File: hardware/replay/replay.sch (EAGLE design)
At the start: 19 parts, among them J1 SQUALL_HEADER, J2 5.5x2.1mm Barrel, U1 LT3083, U2 LT3083, U3 MAX5483

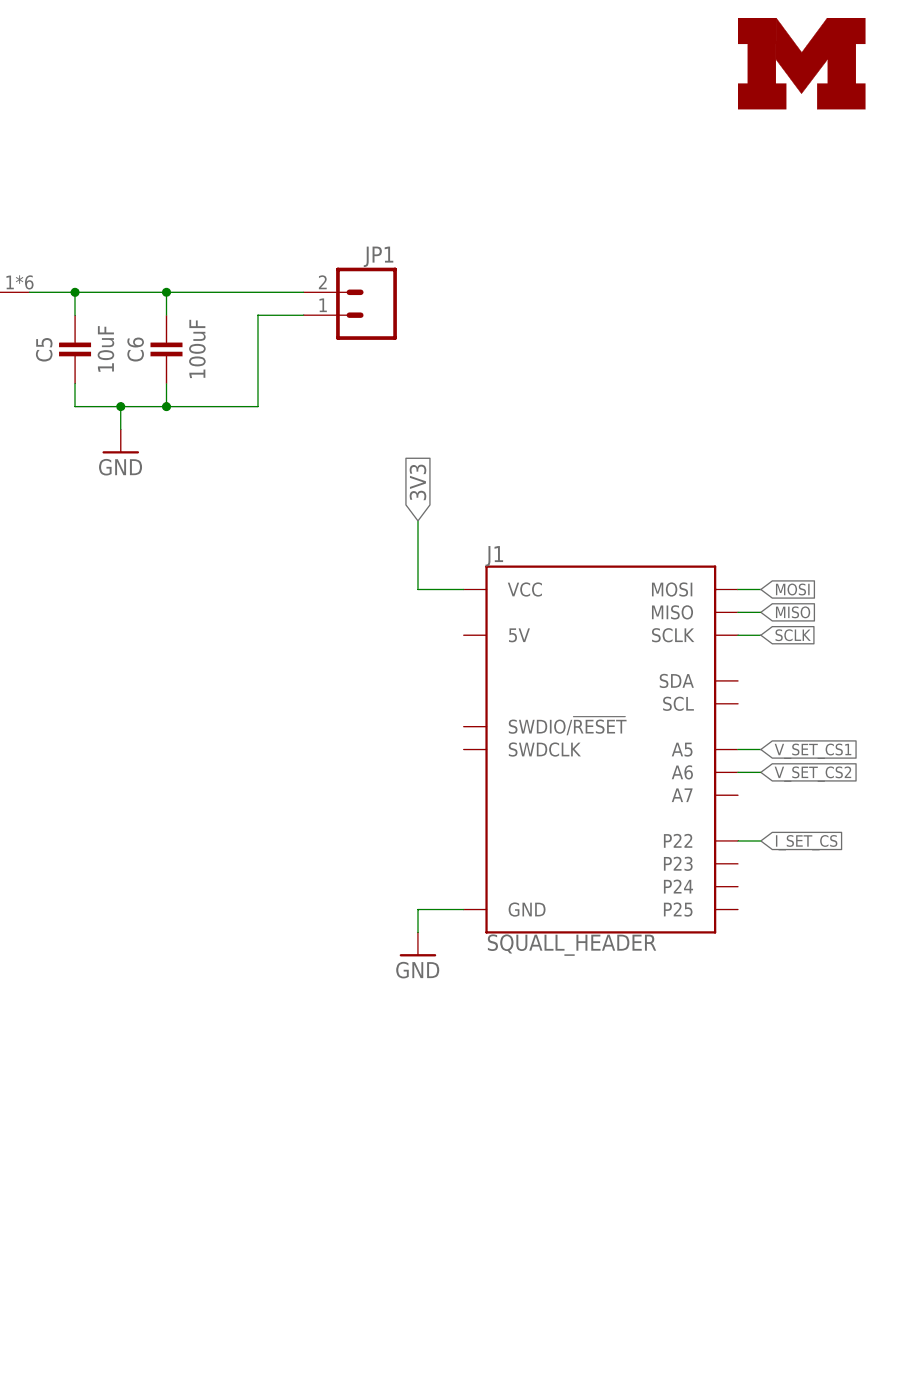
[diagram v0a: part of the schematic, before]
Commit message: board layed out with switches
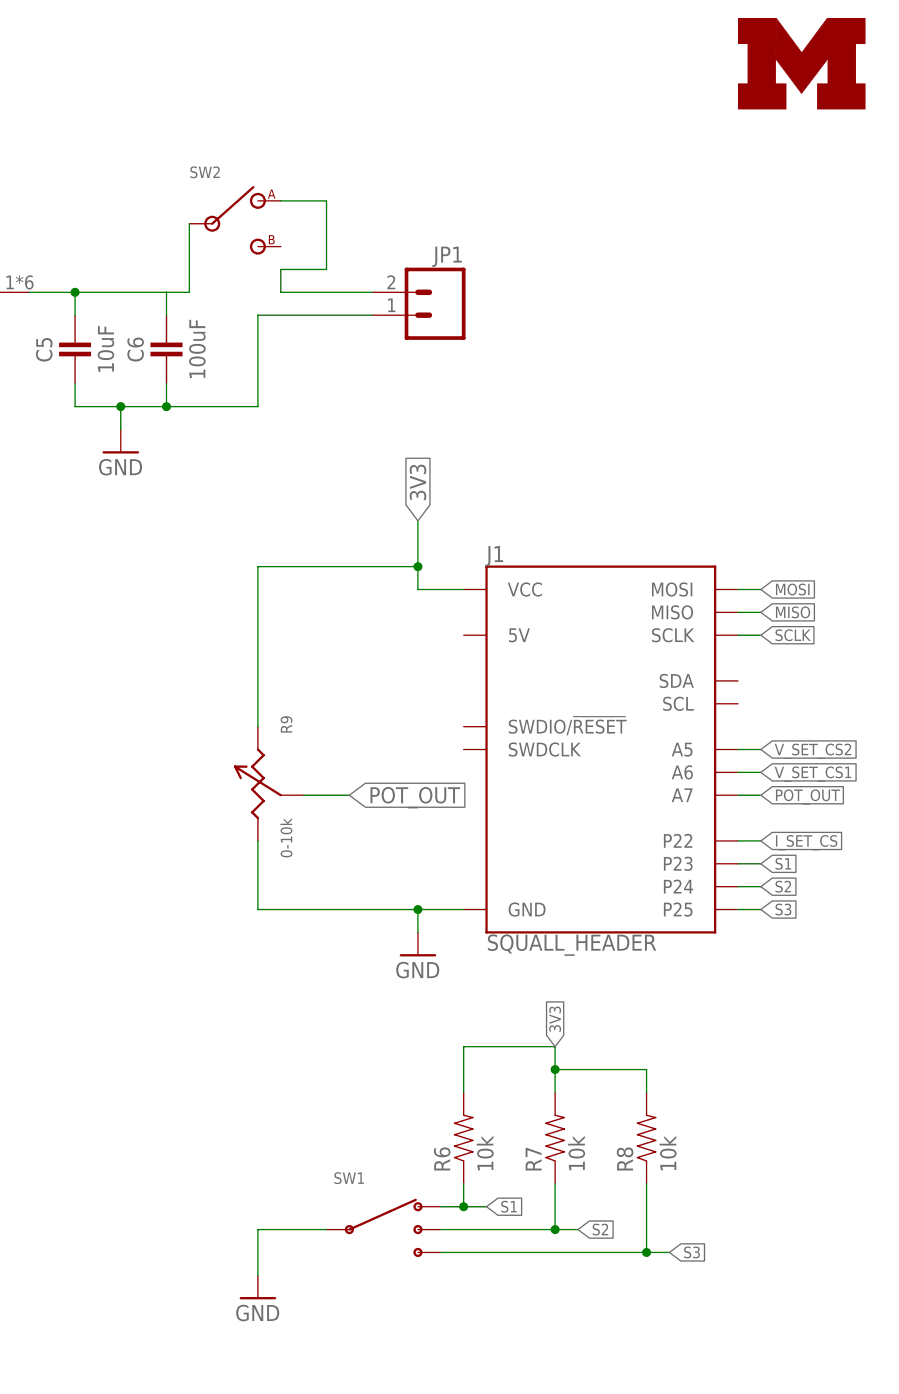
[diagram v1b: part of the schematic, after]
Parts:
- added R6, R7, R8: 10k, passives:RESISTOR
- added R9: 0-10k, pots:POT
- added SW1: CSS-1310TB, switches:CSS-1310TB
- added SW2: 500ASSP, switches:500ASSP
- U3: value MAX5483 -> (none)
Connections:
- new net OUTS: JP1.2, SW2.1
- new net POT_OUT: J1.A7, R9.2
- new net S1: J1.P23, R6.1, SW1.3
- new net S2: J1.P24, R7.1, SW1.2
- new net S3: J1.P25, R8.1, SW1.1
- net 3V3: now also R6.2, R7.2, R8.2, R9.1
- net GND: now also R9.3, SW1.C
- net OUT: now also SW2.2; no longer JP1.2
- net V_SET_CS1: now also J1.A6; no longer J1.A5
- net V_SET_CS2: now also J1.A5; no longer J1.A6
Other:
- moved on the sheet: JP1
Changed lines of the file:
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@@
 <part name="GND9" library="supply1" deviceset="GND" device=""/>
 <part name="JP1" library="SparkFun-Connectors" deviceset="M02" device="5MM"/>
+<part name="SW2" library="switches" deviceset="500ASSP" device=""/>
+<part name="R9" library="pots" deviceset="POT" device="" value="0-10k"/>
+<part name="SW1" library="switches" deviceset="CSS-1310TB" device=""/>
+<part name="GND10" library="supply1" deviceset="GND" device=""/>
+<part name="R6" library="passives" deviceset="RESISTOR" device="" value="10k"/>
+<part name="R7" library="passives" deviceset="RESISTOR" device="" value="10k"/>
+<part name="R8" library="passives" deviceset="RESISTOR" device="" value="10k"/>
 </parts>
 <sheets>
@@
 <instance part="GND8" gate="1" x="116.84" y="142.24"/>
 <instance part="GND9" gate="1" x="162.56" y="134.62"/>
-<instance part="JP1" gate="G$1" x="190.5" y="149.86" rot="MR0"/>
+<instance part="JP1" gate="G$1" x="198.12" y="149.86" rot="MR0"/>
+<instance part="SW2" gate="G$1" x="172.72" y="160.02"/>
+<instance part="R9" gate="G$1" x="177.8" y="99.06" rot="R270"/>
+<instance part="SW1" gate="G$1" x="187.96" y="48.26"/>
+<instance part="GND10" gate="1" x="177.8" y="40.64"/>
+<instance part="R6" gate="G$1" x="200.66" y="58.42" rot="R90"/>
+<instance part="R7" gate="G$1" x="210.82" y="58.42" rot="R90"/>
+<instance part="R8" gate="G$1" x="220.98" y="58.42" rot="R90"/>
 </instances>
 <busses>
@@
 <wire x1="195.58" y1="83.82" x2="195.58" y2="81.28" width="0.1524" layer="91"/>
 <pinref part="GND5" gate="1" pin="GND"/>
+<pinref part="R9" gate="G$1" pin="3"/>
+<wire x1="177.8" y1="91.44" x2="177.8" y2="83.82" width="0.1524" layer="91"/>
+<wire x1="177.8" y1="83.82" x2="195.58" y2="83.82" width="0.1524" layer="91"/>
+<junction x="195.58" y="83.82"/>
 </segment>
 <segment>
@@
 <junction x="167.64" y="139.7"/>
 <pinref part="JP1" gate="G$1" pin="1"/>
-<wire x1="177.8" y1="149.86" x2="182.88" y2="149.86" width="0.1524" layer="91"/>
+<wire x1="177.8" y1="149.86" x2="190.5" y2="149.86" width="0.1524" layer="91"/>
+</segment>
+<segment>
+<pinref part="GND10" gate="1" pin="GND"/>
+<wire x1="177.8" y1="43.18" x2="177.8" y2="48.26" width="0.1524" layer="91"/>
+<pinref part="SW1" gate="G$1" pin="C"/>
+<wire x1="177.8" y1="48.26" x2="185.42" y2="48.26" width="0.1524" layer="91"/>
 </segment>
 </net>
@@
 <pinref part="J1" gate="G$1" pin="VCC"/>
 <wire x1="200.66" y1="119.38" x2="195.58" y2="119.38" width="0.1524" layer="91"/>
-<wire x1="195.58" y1="119.38" x2="195.58" y2="127" width="0.1524" layer="91"/>
+<wire x1="195.58" y1="119.38" x2="195.58" y2="121.92" width="0.1524" layer="91"/>
 <label x="195.58" y="127" size="1.778" layer="95" rot="R90" xref="yes"/>
+<pinref part="R9" gate="G$1" pin="1"/>
+<wire x1="195.58" y1="121.92" x2="195.58" y2="127" width="0.1524" layer="91"/>
+<wire x1="177.8" y1="104.14" x2="177.8" y2="121.92" width="0.1524" layer="91"/>
+<wire x1="177.8" y1="121.92" x2="195.58" y2="121.92" width="0.1524" layer="91"/>
+<junction x="195.58" y="121.92"/>
 </segment>
 <segment>
 <pinref part="R5" gate="G$1" pin="2"/>
 <wire x1="22.86" y1="129.54" x2="22.86" y2="132.08" width="0.1524" layer="91"/>
+</segment>
+<segment>
+<pinref part="R8" gate="G$1" pin="2"/>
+<wire x1="220.98" y1="63.5" x2="220.98" y2="66.04" width="0.1524" layer="91"/>
+<pinref part="R6" gate="G$1" pin="2"/>
+<wire x1="200.66" y1="63.5" x2="200.66" y2="68.58" width="0.1524" layer="91"/>
+<wire x1="200.66" y1="68.58" x2="210.82" y2="68.58" width="0.1524" layer="91"/>
+<pinref part="R7" gate="G$1" pin="2"/>
+<wire x1="210.82" y1="68.58" x2="210.82" y2="66.04" width="0.1524" layer="91"/>
+<wire x1="210.82" y1="66.04" x2="210.82" y2="63.5" width="0.1524" layer="91"/>
+<wire x1="220.98" y1="66.04" x2="210.82" y2="66.04" width="0.1524" layer="91"/>
+<junction x="210.82" y="66.04"/>
+<label x="210.82" y="68.58" size="1.27" layer="95" rot="R90" xref="yes"/>
 </segment>
 </net>
@@
 </segment>
 <segment>
+<pinref part="J1" gate="G$1" pin="A6"/>
+<wire x1="231.14" y1="99.06" x2="233.68" y2="99.06" width="0.1524" layer="91"/>
+<label x="233.68" y="99.06" size="1.27" layer="95" xref="yes"/>
+</segment>
+</net>
+<net name="V_SET_CS2" class="0">
+<segment>
+<pinref part="R3" gate="G$1" pin="!CS"/>
+<wire x1="109.22" y1="71.12" x2="106.68" y2="71.12" width="0.1524" layer="91"/>
+<label x="106.68" y="71.12" size="1.778" layer="95" rot="R180" xref="yes"/>
+</segment>
+<segment>
 <pinref part="J1" gate="G$1" pin="A5"/>
 <wire x1="231.14" y1="101.6" x2="233.68" y2="101.6" width="0.1524" layer="91"/>
 <label x="233.68" y="101.6" size="1.27" layer="95" xref="yes"/>
-</segment>
-</net>
-<net name="V_SET_CS2" class="0">
-<segment>
-<pinref part="R3" gate="G$1" pin="!CS"/>
-<wire x1="109.22" y1="71.12" x2="106.68" y2="71.12" width="0.1524" layer="91"/>
-<label x="106.68" y="71.12" size="1.778" layer="95" rot="R180" xref="yes"/>
-</segment>
-<segment>
-<pinref part="J1" gate="G$1" pin="A6"/>
-<wire x1="231.14" y1="99.06" x2="233.68" y2="99.06" width="0.1524" layer="91"/>
-<label x="233.68" y="99.06" size="1.27" layer="95" xref="yes"/>
 </segment>
 </net>
@@
 <pinref part="C6" gate="G$1" pin="1"/>
 <wire x1="167.64" y1="149.86" x2="167.64" y2="152.4" width="0.1524" layer="91"/>
-<pinref part="JP1" gate="G$1" pin="2"/>
-<wire x1="167.64" y1="152.4" x2="182.88" y2="152.4" width="0.1524" layer="91"/>
-<junction x="167.64" y="152.4"/>
+<wire x1="167.64" y1="152.4" x2="170.18" y2="152.4" width="0.1524" layer="91"/>
+<wire x1="170.18" y1="152.4" x2="170.18" y2="160.02" width="0.1524" layer="91"/>
+<pinref part="SW2" gate="G$1" pin="2"/>
 </segment>
 </net>
@@
 </segment>
 </net>
+<net name="OUTS" class="0">
+<segment>
+<wire x1="180.34" y1="162.56" x2="185.42" y2="162.56" width="0.1524" layer="91"/>
+<wire x1="185.42" y1="162.56" x2="185.42" y2="154.94" width="0.1524" layer="91"/>
+<wire x1="185.42" y1="154.94" x2="180.34" y2="154.94" width="0.1524" layer="91"/>
+<wire x1="180.34" y1="154.94" x2="180.34" y2="152.4" width="0.1524" layer="91"/>
+<pinref part="JP1" gate="G$1" pin="2"/>
+<wire x1="180.34" y1="152.4" x2="190.5" y2="152.4" width="0.1524" layer="91"/>
+<pinref part="SW2" gate="G$1" pin="1"/>
+</segment>
+</net>
+<net name="POT_OUT" class="0">
+<segment>
+<wire x1="182.88" y1="96.52" x2="187.96" y2="96.52" width="0.1524" layer="91"/>
+<label x="187.96" y="96.52" size="1.778" layer="95" xref="yes"/>
+<pinref part="R9" gate="G$1" pin="2"/>
+</segment>
+<segment>
+<pinref part="J1" gate="G$1" pin="A7"/>
+<wire x1="231.14" y1="96.52" x2="233.68" y2="96.52" width="0.1524" layer="91"/>
+<label x="233.68" y="96.52" size="1.27" layer="95" xref="yes"/>
+</segment>
+</net>
+<net name="S1" class="0">
+<segment>
+<pinref part="SW1" gate="G$1" pin="3"/>
+<wire x1="198.12" y1="50.8" x2="200.66" y2="50.8" width="0.1524" layer="91"/>
+<label x="203.2" y="50.8" size="1.27" layer="95" xref="yes"/>
+<pinref part="R6" gate="G$1" pin="1"/>
+<wire x1="200.66" y1="50.8" x2="203.2" y2="50.8" width="0.1524" layer="91"/>
+<wire x1="200.66" y1="53.34" x2="200.66" y2="50.8" width="0.1524" layer="91"/>
+<junction x="200.66" y="50.8"/>
+</segment>
+<segment>
+<pinref part="J1" gate="G$1" pin="P23"/>
+<wire x1="231.14" y1="88.9" x2="233.68" y2="88.9" width="0.1524" layer="91"/>
+<label x="233.68" y="88.9" size="1.27" layer="95" xref="yes"/>
+</segment>
+</net>
+<net name="S2" class="0">
+<segment>
+<pinref part="SW1" gate="G$1" pin="2"/>
+<wire x1="198.12" y1="48.26" x2="210.82" y2="48.26" width="0.1524" layer="91"/>
+<label x="213.36" y="48.26" size="1.27" layer="95" xref="yes"/>
+<pinref part="R7" gate="G$1" pin="1"/>
+<wire x1="210.82" y1="48.26" x2="213.36" y2="48.26" width="0.1524" layer="91"/>
+<wire x1="210.82" y1="53.34" x2="210.82" y2="48.26" width="0.1524" layer="91"/>
+<junction x="210.82" y="48.26"/>
+</segment>
+<segment>
+<pinref part="J1" gate="G$1" pin="P24"/>
+<wire x1="231.14" y1="86.36" x2="233.68" y2="86.36" width="0.1524" layer="91"/>
+<label x="233.68" y="86.36" size="1.27" layer="95" xref="yes"/>
+</segment>
+</net>
+<net name="S3" class="0">
+<segment>
+<pinref part="SW1" gate="G$1" pin="1"/>
+<wire x1="198.12" y1="45.72" x2="220.98" y2="45.72" width="0.1524" layer="91"/>
+<label x="223.52" y="45.72" size="1.27" layer="95" xref="yes"/>
+<pinref part="R8" gate="G$1" pin="1"/>
+<wire x1="220.98" y1="45.72" x2="223.52" y2="45.72" width="0.1524" layer="91"/>
+<wire x1="220.98" y1="53.34" x2="220.98" y2="45.72" width="0.1524" layer="91"/>
+<junction x="220.98" y="45.72"/>
+</segment>
+<segment>
+<pinref part="J1" gate="G$1" pin="P25"/>
+<wire x1="231.14" y1="83.82" x2="233.68" y2="83.82" width="0.1524" layer="91"/>
+<label x="233.68" y="83.82" size="1.27" layer="95" xref="yes"/>
+</segment>
+</net>

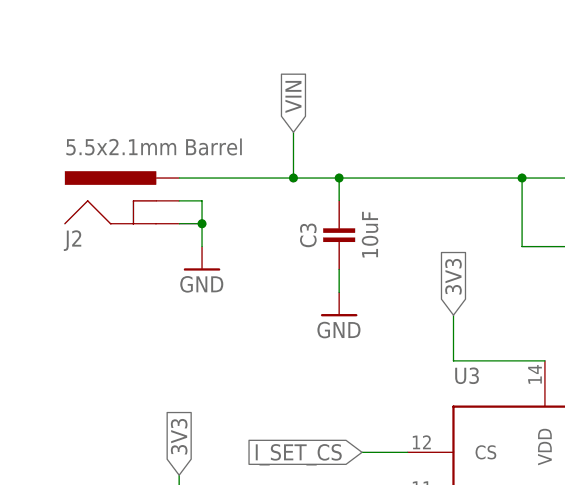
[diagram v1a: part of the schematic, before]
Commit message: updated parts on the board and started making a case
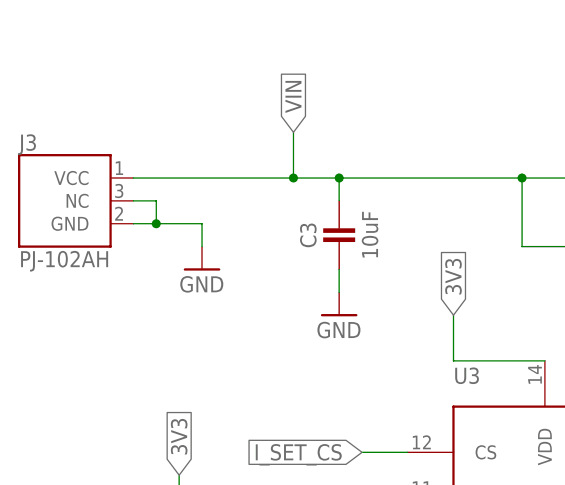
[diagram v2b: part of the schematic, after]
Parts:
- removed J2: 5.5x2.1mm Barrel, SparkFun-Connectors:POWER_JACKSMD
- added J3: PJ-102AH, connector:PJ-102AH
- SW1: value CSS-1310TB -> OS103011; device switches:CSS-1310TB -> switches:OS103011
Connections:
- net GND: now also J3.GND, J3.NC; no longer J2.GND, J2.GNDBREAK
- net VIN: now also J3.VCC; no longer J2.PWR
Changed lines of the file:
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@@
 <part name="U3" library="chips" deviceset="MAX5483" device=""/>
 <part name="GND1" library="supply1" deviceset="GND" device=""/>
-<part name="J2" library="SparkFun-Connectors" deviceset="POWER_JACK" device="SMD" value="5.5x2.1mm Barrel"/>
 <part name="R2" library="chips" deviceset="MAX5424" device=""/>
 <part name="R3" library="chips" deviceset="MAX5424" device=""/>
@@
 <part name="SW2" library="switches" deviceset="500ASSP" device=""/>
 <part name="R9" library="pots" deviceset="POT" device="" value="0-10k"/>
-<part name="SW1" library="switches" deviceset="CSS-1310TB" device=""/>
 <part name="GND10" library="supply1" deviceset="GND" device=""/>
 <part name="R6" library="passives" deviceset="RESISTOR" device="" value="10k"/>
 <part name="R7" library="passives" deviceset="RESISTOR" device="" value="10k"/>
 <part name="R8" library="passives" deviceset="RESISTOR" device="" value="10k"/>
+<part name="J3" library="connector" deviceset="PJ-102AH" device=""/>
+<part name="SW1" library="switches" deviceset="OS103011" device=""/>
 </parts>
 <sheets>
@@
 <instance part="U3" gate="G$1" x="63.5" y="129.54"/>
 <instance part="GND1" gate="1" x="58.42" y="91.44"/>
-<instance part="J2" gate="G$1" x="20.32" y="157.48"/>
 <instance part="R2" gate="G$1" x="124.46" y="127"/>
 <instance part="R3" gate="G$1" x="124.46" y="81.28"/>
@@
 <instance part="SW2" gate="G$1" x="172.72" y="160.02"/>
 <instance part="R9" gate="G$1" x="177.8" y="99.06" rot="R270"/>
-<instance part="SW1" gate="G$1" x="187.96" y="48.26"/>
 <instance part="GND10" gate="1" x="177.8" y="40.64"/>
 <instance part="R6" gate="G$1" x="200.66" y="58.42" rot="R90"/>
 <instance part="R7" gate="G$1" x="210.82" y="58.42" rot="R90"/>
 <instance part="R8" gate="G$1" x="220.98" y="58.42" rot="R90"/>
+<instance part="J3" gate="G$1" x="10.16" y="162.56"/>
+<instance part="SW1" gate="G$1" x="187.96" y="48.26"/>
 </instances>
 <busses>
@@
 </segment>
 <segment>
-<pinref part="J2" gate="G$1" pin="GND"/>
 <pinref part="GND6" gate="1" pin="GND"/>
-<wire x1="22.86" y1="160.02" x2="25.4" y2="160.02" width="0.1524" layer="91"/>
+<pinref part="J3" gate="G$1" pin="GND"/>
+<wire x1="17.78" y1="160.02" x2="20.32" y2="160.02" width="0.1524" layer="91"/>
+<wire x1="20.32" y1="160.02" x2="25.4" y2="160.02" width="0.1524" layer="91"/>
 <wire x1="25.4" y1="160.02" x2="25.4" y2="157.48" width="0.1524" layer="91"/>
-<pinref part="J2" gate="G$1" pin="GNDBREAK"/>
-<wire x1="22.86" y1="162.56" x2="25.4" y2="162.56" width="0.1524" layer="91"/>
-<wire x1="25.4" y1="162.56" x2="25.4" y2="160.02" width="0.1524" layer="91"/>
-<junction x="25.4" y="160.02"/>
+<pinref part="J3" gate="G$1" pin="NC"/>
+<wire x1="17.78" y1="162.56" x2="20.32" y2="162.56" width="0.1524" layer="91"/>
+<wire x1="20.32" y1="162.56" x2="20.32" y2="160.02" width="0.1524" layer="91"/>
+<junction x="20.32" y="160.02"/>
 </segment>
 <segment>
@@
 <pinref part="GND10" gate="1" pin="GND"/>
 <wire x1="177.8" y1="43.18" x2="177.8" y2="48.26" width="0.1524" layer="91"/>
+<wire x1="177.8" y1="48.26" x2="185.42" y2="48.26" width="0.1524" layer="91"/>
 <pinref part="SW1" gate="G$1" pin="C"/>
-<wire x1="177.8" y1="48.26" x2="185.42" y2="48.26" width="0.1524" layer="91"/>
 </segment>
 </net>
 <net name="VIN" class="0">
 <segment>
-<pinref part="J2" gate="G$1" pin="PWR"/>
 <pinref part="U1" gate="G$1" pin="VIN"/>
-<wire x1="22.86" y1="165.1" x2="35.56" y2="165.1" width="0.1524" layer="91"/>
 <wire x1="35.56" y1="165.1" x2="40.64" y2="165.1" width="0.1524" layer="91"/>
 <wire x1="40.64" y1="165.1" x2="60.96" y2="165.1" width="0.1524" layer="91"/>
@@
 <wire x1="40.64" y1="165.1" x2="40.64" y2="162.56" width="0.1524" layer="91"/>
 <junction x="40.64" y="165.1"/>
+<wire x1="35.56" y1="165.1" x2="17.78" y2="165.1" width="0.1524" layer="91"/>
+<pinref part="J3" gate="G$1" pin="VCC"/>
 </segment>
 <segment>
@@
 <net name="S1" class="0">
 <segment>
-<pinref part="SW1" gate="G$1" pin="3"/>
 <wire x1="198.12" y1="50.8" x2="200.66" y2="50.8" width="0.1524" layer="91"/>
 <label x="203.2" y="50.8" size="1.27" layer="95" xref="yes"/>
@@
 <wire x1="200.66" y1="53.34" x2="200.66" y2="50.8" width="0.1524" layer="91"/>
 <junction x="200.66" y="50.8"/>
+<pinref part="SW1" gate="G$1" pin="3"/>
 </segment>
 <segment>
@@
 <net name="S2" class="0">
 <segment>
-<pinref part="SW1" gate="G$1" pin="2"/>
 <wire x1="198.12" y1="48.26" x2="210.82" y2="48.26" width="0.1524" layer="91"/>
 <label x="213.36" y="48.26" size="1.27" layer="95" xref="yes"/>
@@
 <wire x1="210.82" y1="53.34" x2="210.82" y2="48.26" width="0.1524" layer="91"/>
 <junction x="210.82" y="48.26"/>
+<pinref part="SW1" gate="G$1" pin="2"/>
 </segment>
 <segment>
@@
 <net name="S3" class="0">
 <segment>
-<pinref part="SW1" gate="G$1" pin="1"/>
 <wire x1="198.12" y1="45.72" x2="220.98" y2="45.72" width="0.1524" layer="91"/>
 <label x="223.52" y="45.72" size="1.27" layer="95" xref="yes"/>
@@
 <wire x1="220.98" y1="53.34" x2="220.98" y2="45.72" width="0.1524" layer="91"/>
 <junction x="220.98" y="45.72"/>
-</segment>
-<segment>
+<pinref part="SW1" gate="G$1" pin="1"/>
+</segment>
+<segment>
